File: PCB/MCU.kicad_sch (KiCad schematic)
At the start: 26 parts, among them J1 TC2030-NL, J2 VIK Keyboard Expansion, J3 SWD, Q1 AO3400A, Q2 AO3400A, SW2 Reset, U1 STM32F072RBT6

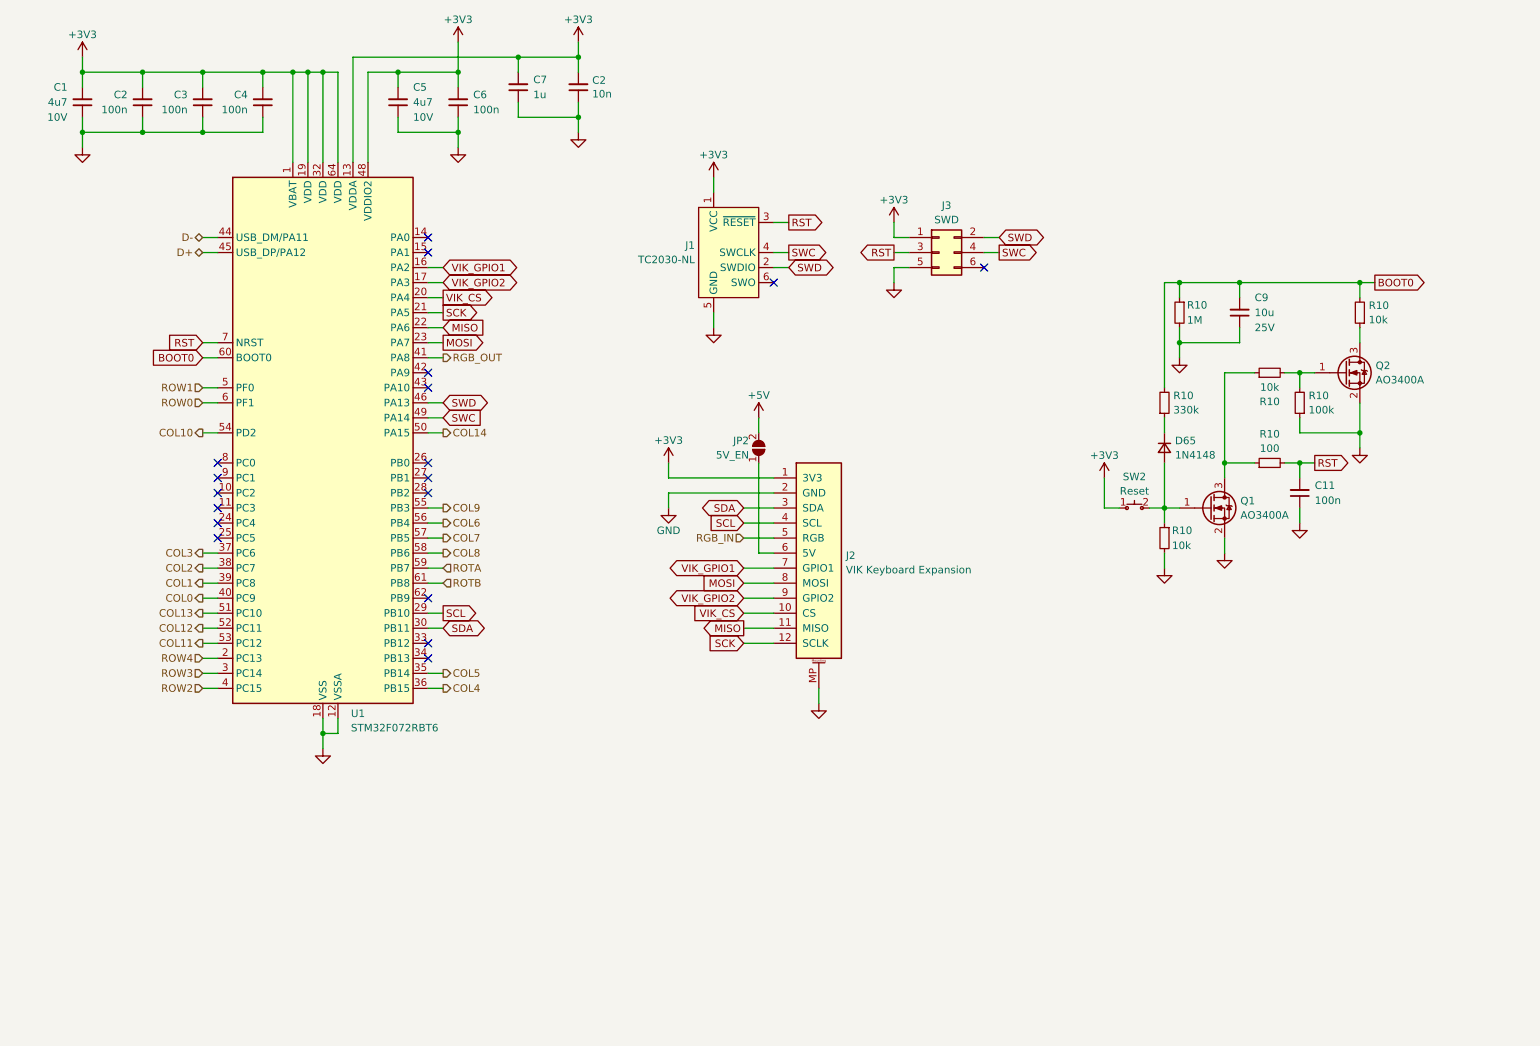
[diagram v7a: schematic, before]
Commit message: 28/08/2023 update
Added test points for VIK connector. Refined case and scrollwheel design. Added pull-up resistor to RGB trace. Added Acheron single-push reset circuit. Updated STEP files.
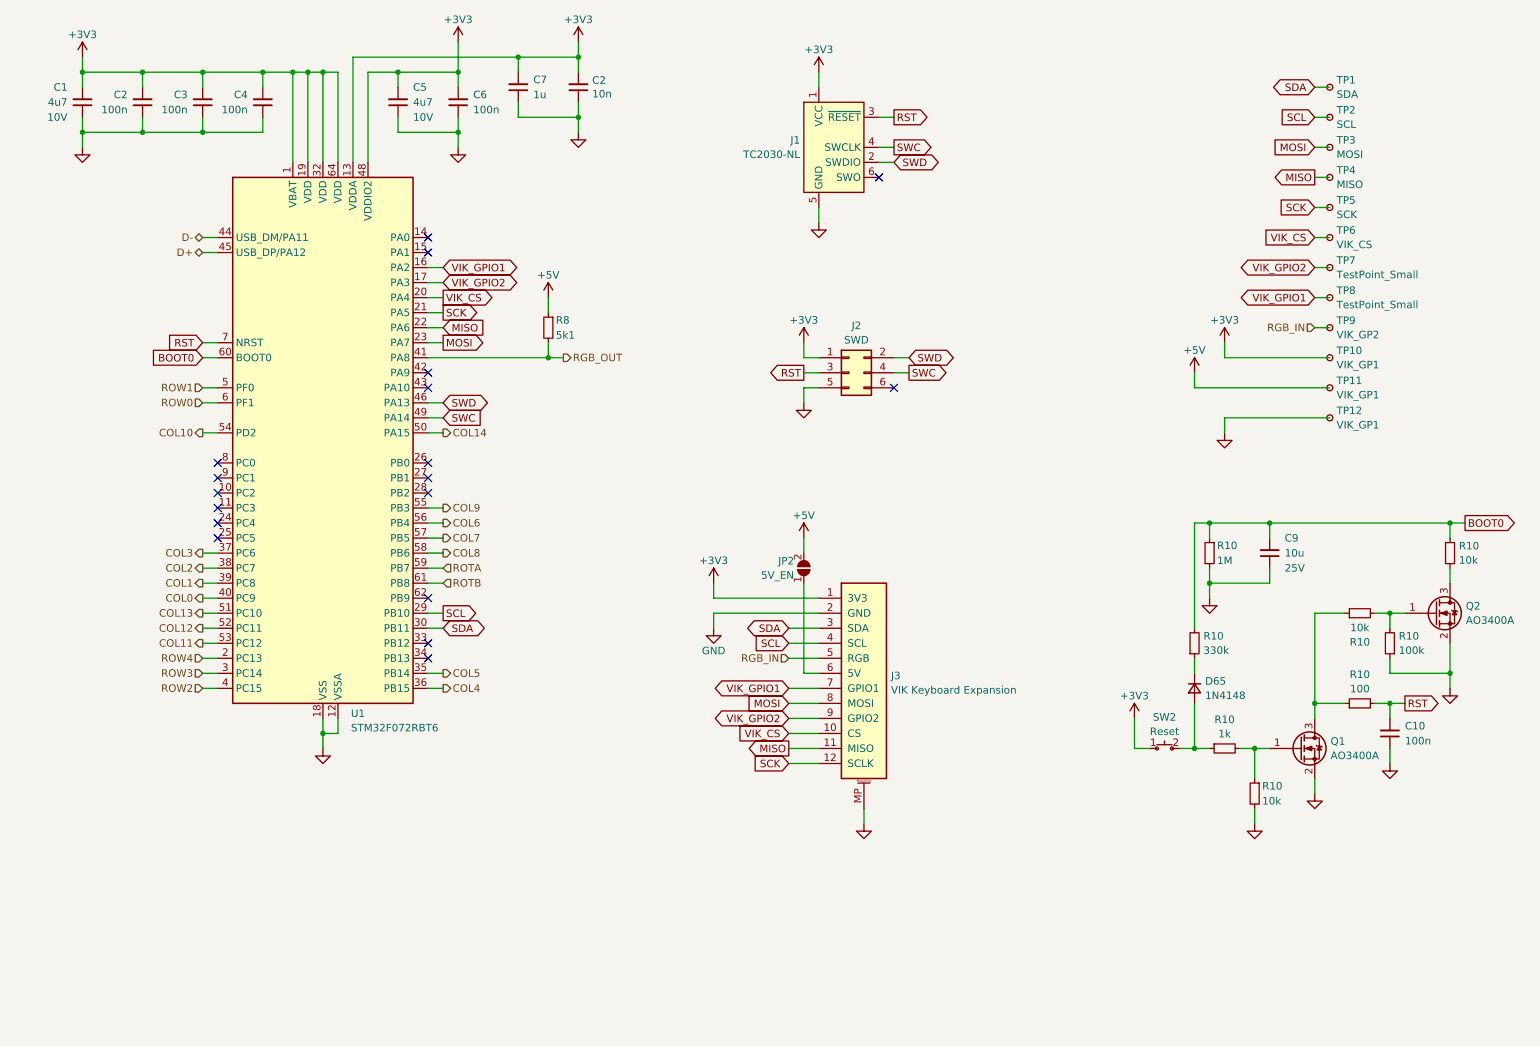
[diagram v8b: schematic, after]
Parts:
- added R10: 1k, Ariamelon-Device:R_0402_1005Metric, symbol Device:R_Small
- added R8: 5k1, Ariamelon-Device:R_0402_1005Metric, symbol Device:R_Small
- added TP1: SDA, Ariamelon-HolePad:TestPoint_Pad_D1.5mm, symbol Connector:TestPoint_Small
- added TP10, TP11, TP12: VIK_GP1, Ariamelon-HolePad:TestPoint_Pad_D1.5mm, symbol Connector:TestPoint_Small
- added TP2: SCL, Ariamelon-HolePad:TestPoint_Pad_D1.5mm, symbol Connector:TestPoint_Small
- added TP3: MOSI, Ariamelon-HolePad:TestPoint_Pad_D1.5mm, symbol Connector:TestPoint_Small
- added TP4: MISO, Ariamelon-HolePad:TestPoint_Pad_D1.5mm, symbol Connector:TestPoint_Small
- added TP5: SCK, Ariamelon-HolePad:TestPoint_Pad_D1.5mm, symbol Connector:TestPoint_Small
- added TP6: VIK_CS, Ariamelon-HolePad:TestPoint_Pad_D1.5mm, symbol Connector:TestPoint_Small
- added TP7, TP8: TestPoint_Small, Ariamelon-HolePad:TestPoint_Pad_D1.5mm, symbol Connector:TestPoint_Small
- added TP9: VIK_GP2, Ariamelon-HolePad:TestPoint_Pad_D1.5mm, symbol Connector:TestPoint_Small
- renumbered C11 to C10, J3 to J2, J2 to J3
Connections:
- net +3V3: now also TP10.1
- net +5V: now also R8.1, TP11.1
- net GND: now also TP12.1
- net MISO: now also TP4.1
- net MOSI: now also TP3.1
- net RGB_IN: now also TP9.1
- net RGB_OUT: now also R8.2
- net SCK: now also TP5.1
- net SCL: now also TP2.1
- net SDA: now also TP1.1
- net VIK_CS: now also TP6.1
- net VIK_GPIO1: now also TP8.1
- net VIK_GPIO2: now also TP7.1
- net at D65.2 (A), SW2.2 (B): now also R10.1; no longer Q1.1 (G), R10.1
- new net: Q1.1 (G), R10.1, R10.2
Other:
- moved on the sheet: C10, C9, D65, J1, J2, J3, JP2, Q1, Q2, R10, SW2
